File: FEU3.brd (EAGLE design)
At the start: 79.4 x 81.7 mm, 56 parts, among them IC1 LM358N, Q1 8M, Q2 32748

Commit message: New BRD 2
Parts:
- moved R4 67.6 mm to (8.11, 39.6), turned to 90 degrees
- moved UART_USB 64.6 mm to (5.91, 65.1)
- moved U$2 58.8 mm to (65.9, 44.1)
- moved FEU1 58.1 mm to (66.0, 28.0)
- moved FEU2 58.0 mm to (66.0, 34.9)
- moved U$5 57.5 mm to (8.36, 33.6)
- moved U$3 57.2 mm to (65.9, 15.6)
- moved R11 52.0 mm to (11.9, 15.9)
- moved R15 49.5 mm to (8.09, 33.8), turned to 90 degrees
- moved R9 47.3 mm to (56.4, 44.8), turned to 90 degrees
- moved C14 46.6 mm to (58.9, 44.9), turned to 270 degrees
- moved R7 46.3 mm to (62.7, 22.5)
- moved R16 39.7 mm to (17.1, 29.4), turned to 270 degrees
- moved C16 37.6 mm to (53.9, 26.4)
- moved C10 35.7 mm to (22.1, 37.1)
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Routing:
- net GND: track 0.00 -> 179.1 mm, vias 0 -> 6
- net 3.3V: track 0.00 -> 98.3 mm, vias 0 -> 2
- net USART_RX_STM: track 0.00 -> 56.1 mm
- net S2: track 0.00 -> 34.3 mm
- net N$17: track 0.00 -> 28.5 mm
- net S1: track 0.00 -> 25.8 mm
- net N$8: track 0.00 -> 24.9 mm, vias 0 -> 1
- net NRST: track 0.00 -> 21.6 mm, vias 0 -> 1
- net S3: track 0.00 -> 20.3 mm, vias 0 -> 1
- net ADC_S: track 0.00 -> 17.6 mm
- net SWDAT: track 0.00 -> 15.7 mm
- net SWCLK: track 0.00 -> 15.0 mm
- net N$14: track 0.00 -> 14.5 mm
- net N$15: track 0.00 -> 12.7 mm, vias 0 -> 1
- net N$13: track 0.00 -> 12.5 mm
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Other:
- board outline removed

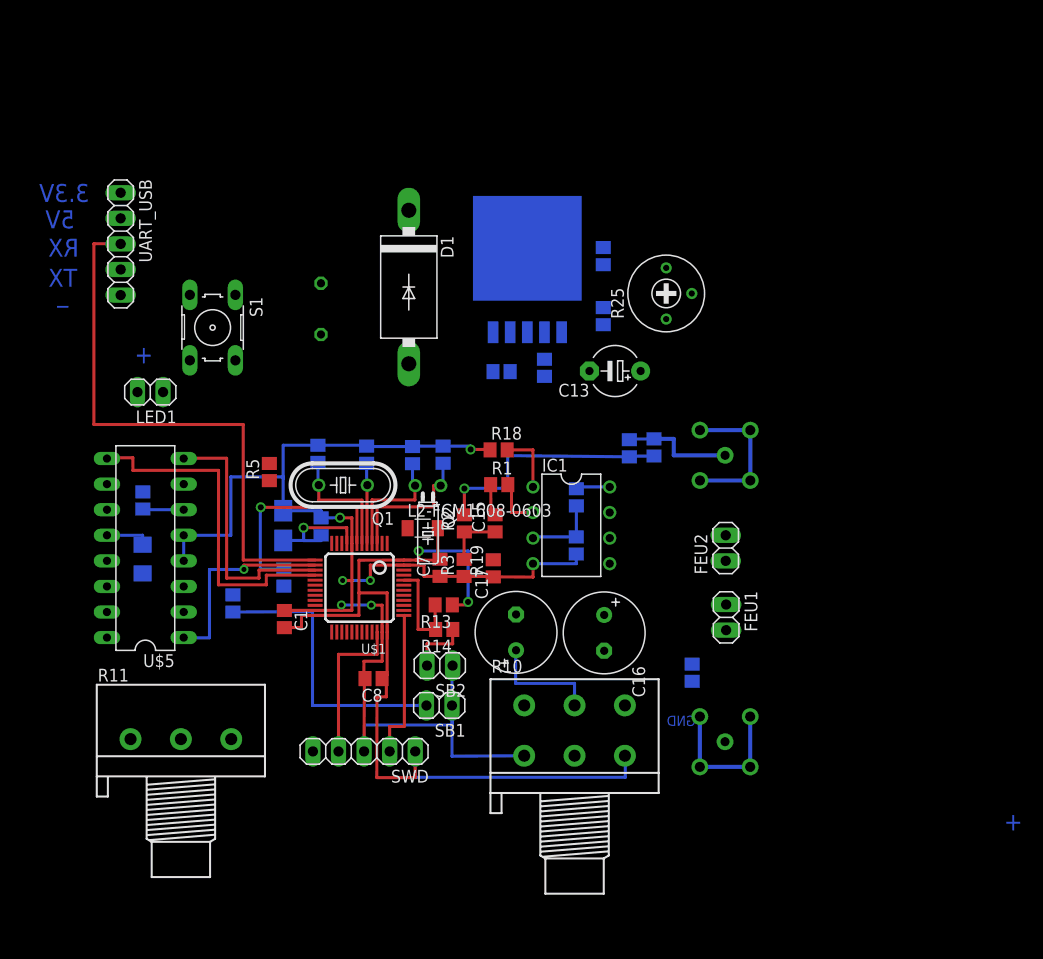
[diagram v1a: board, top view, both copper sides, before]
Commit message: Schematic and board for factory v.1
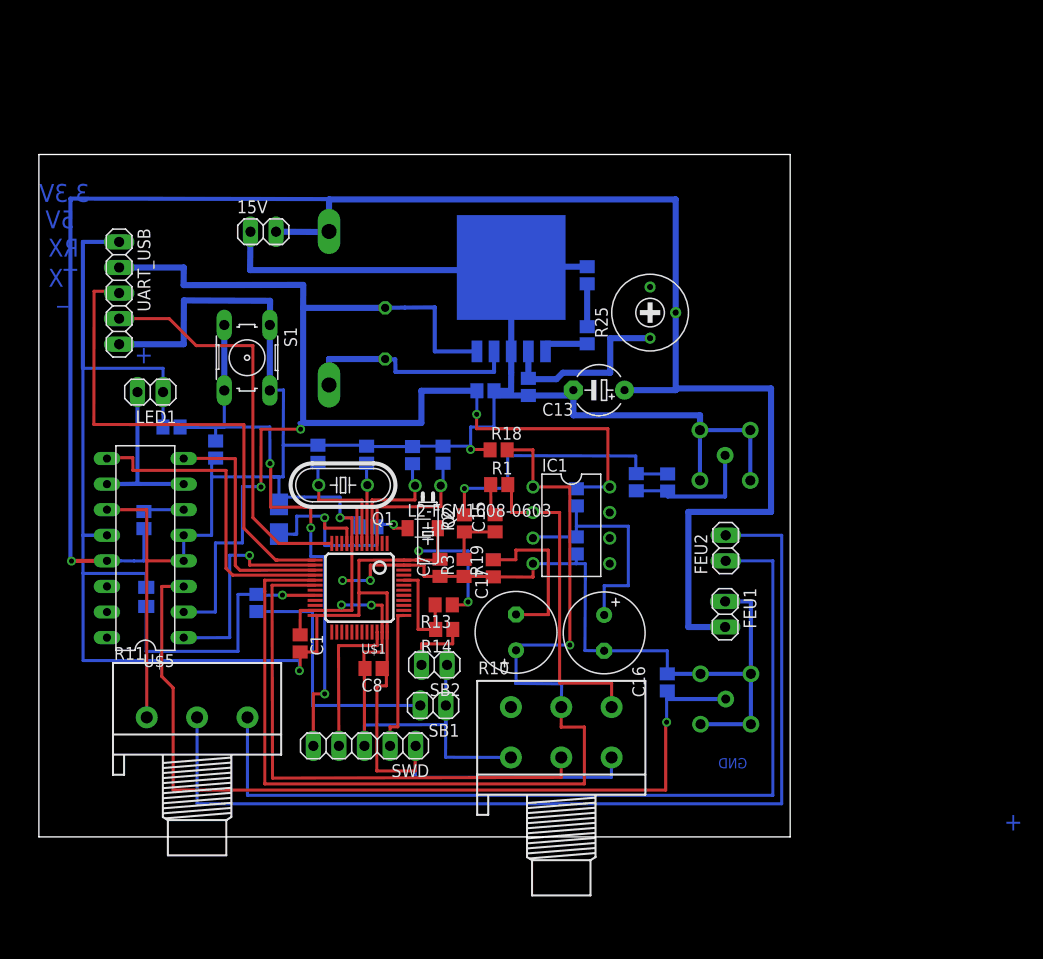
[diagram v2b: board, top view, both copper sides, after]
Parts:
- added 15V: (no value), pinhead:1X02
- R15: device resistor:R1206 -> resistor:M0805
- moved C9 14.4 mm to (15.3, 44.6)
- moved R5 10.7 mm to (11.0, 46.9), flipped to the bottom, turned to 0 degrees
- moved D1 8.19 mm to (26.6, 58.7), flipped to the bottom
- moved L2 6.82 mm to (32.2, 56.2)
- moved UART_USB 4.88 mm to (5.76, 60.2)
- moved C2 4.70 mm to (30.5, 37.0), turned to 180 degrees
- moved S1 4.54 mm to (18.5, 53.8)
- moved U$3 4.24 mm to (66.0, 19.9)
- moved R15 3.78 mm to (8.45, 30.0)
- moved C14 3.73 mm to (60.2, 41.4), turned to 90 degrees
- moved R9 3.44 mm to (57.1, 41.4), turned to 270 degrees
- moved C1 2.88 mm to (23.7, 25.4)
- moved R11 2.69 mm to (13.5, 18.1)
- moved R7 2.65 mm to (60.2, 21.5), turned to 270 degrees
- moved C13 2.48 mm to (53.4, 50.5)
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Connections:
- net 15V: now also 15V.2
- net GND: now also 15V.1
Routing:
- net GND: track 179.1 -> 368.3 mm
- net 15V: track 0.00 -> 187.3 mm, vias 0 -> 1
- net USB+: track 3.49 -> 132.9 mm, vias 0 -> 3
- net WHITE: track 0.00 -> 98.8 mm
- net 3.3V: track 98.3 -> 191.0 mm, vias 2 -> 3
- net ADC_S: track 17.6 -> 108.6 mm, vias 0 -> 1
- net BLUE: track 0.00 -> 87.9 mm
- net N$23: track 0.00 -> 87.8 mm, vias 0 -> 1
- net ADC_RES: track 0.00 -> 54.1 mm
- net NRST: track 21.6 -> 71.8 mm, vias 1 -> 3
- net UART_TX_STM: track 0.00 -> 40.4 mm
- net N$11: track 5.27 -> 32.4 mm
- net N$19: track 0.00 -> 27.0 mm, vias 0 -> 1
- net N$31: track 0.00 -> 22.2 mm
- net N$4: track 0.00 -> 20.2 mm
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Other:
- board outline added: 74.6 x 67.8 mm
